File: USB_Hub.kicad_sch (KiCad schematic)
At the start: 48 parts, among them U4 VL822-QFN76, U5 AP7361-10ER-13, Y1 25MHz

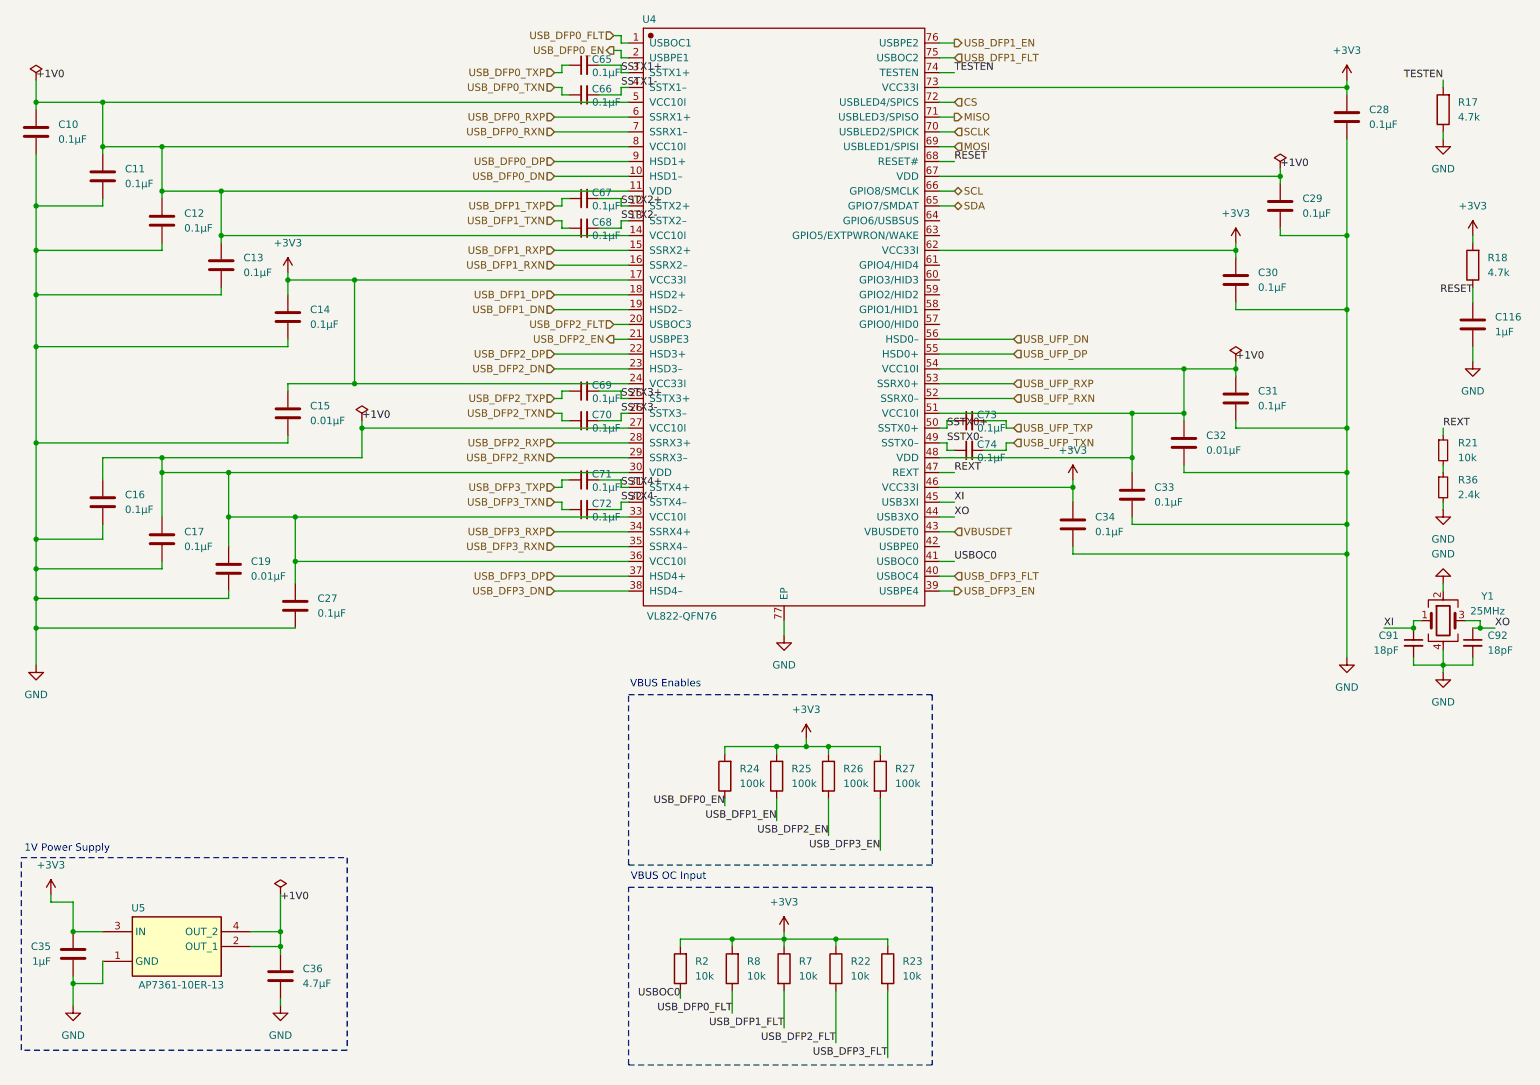
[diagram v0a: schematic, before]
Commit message: pcb: connect SPI flash to VIA IC
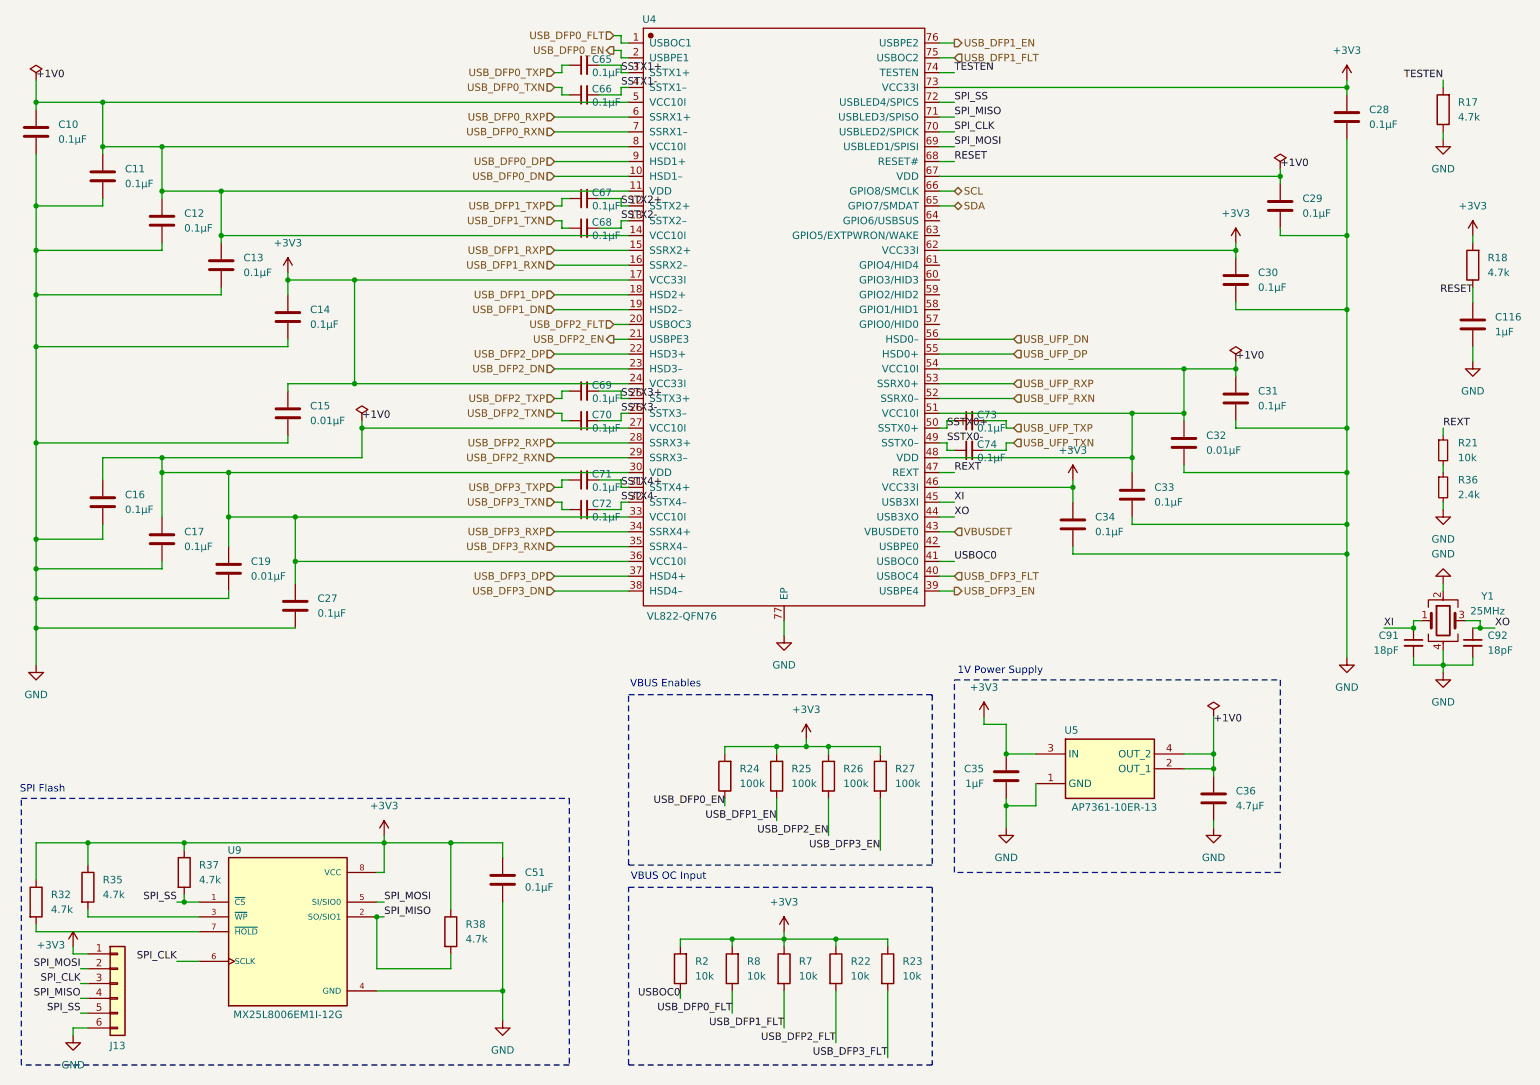
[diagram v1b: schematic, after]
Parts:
- added C51: 0.1µF, Capacitor_SMD:C_0402_1005Metric, symbol Device:C
- added J13: Conn_01x06, Connector_PinHeader_2.54mm:PinHeader_1x06_P2.54mm_Vertical, symbol Connector_Generic:Conn_01x06
- added R32, R35, R37, R38: 4.7k, Resistor_SMD:R_0402_1005Metric, symbol Device:R
- added U9: MX25L8006EM1I-12G, MX25L8006EM1I-12G:MX25L8006EM1I-12G, symbol MX25L8006EM1I-12G:MX25L8006EM1I-12G
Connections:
- net +3V3: now also C51.1, J13.1 (Pin_1), R32.1, R35.1, R37.1, R38.1, U9.8 (VCC)
- net GND: now also C51.2, J13.6 (Pin_6), U9.4 (GND)
- net CS renamed SPI_SS
- net SPI_SS: now also J13.5 (Pin_5), R37.2, U9.1 (~{CS})
- net MISO renamed SPI_MISO
- net SPI_MISO: now also J13.4 (Pin_4), R38.2, U9.2 (SO/SIO1)
- net MOSI renamed SPI_MOSI
- net SPI_MOSI: now also J13.2 (Pin_2), U9.5 (SI/SIO0)
- net SCLK renamed SPI_CLK
- net SPI_CLK: now also J13.3 (Pin_3), U9.6 (SCLK)
- new net: R35.2, U9.3 (~{WP})
- new net: R32.2, U9.7 (~{HOLD})
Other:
- note added: "SPI Flash"
- moved on the sheet: C35, C36, U5
